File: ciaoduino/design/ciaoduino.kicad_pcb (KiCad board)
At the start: 2 copper layers, 8 parts, among them P1 ICSP, SW1 SW_PUSH, SW2 SW_PUSH, X1 CRYSTAL_SMD

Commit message: Make more realistic board.
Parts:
- added P2: CONN_01X02, Pin_Headers:Pin_Header_Angled_1x02, F.Cu at (142.2, 64.8)
- added P3: USB_OTG, Connect:USB_Mini-B, F.Cu at (130.8, 72.4)
- added P4: CONN_01X06, Pin_Headers:Pin_Header_Straight_1x06, F.Cu at (154.9, 95.2)
- added R3: R, Resistors_SMD:R_0603, F.Cu at (139.7, 73.7)
- added R4: R, Resistors_SMD:R_0603, F.Cu at (139.7, 71.1)
- added U2: ATmega32U4-AU, Housings_QFP:TQFP-44_10x10mm_Pitch0.8mm, F.Cu at (151.1, 74.9)
- C1, C2: footprint Capacitors_SMD:C_0603_HandSoldering -> Capacitors_SMD:C_0603
- R1, R2: footprint Resistors_SMD:R_0603_HandSoldering -> Resistors_SMD:R_0603
- moved R2 52.9 mm to (165.1, 67.3)
- moved SW1 39.8 mm to (170.2, 81.3)
- moved R1 31.2 mm to (165.1, 87.6)
- moved C1 25.7 mm to (156.2, 90.2), turned to 270 degrees
- moved SW2 24.0 mm to (170.2, 72.4)
- moved C2 21.8 mm to (146.1, 90.2), turned to 270 degrees
- moved X1 15.1 mm to (151.1, 90.2), turned to 180 degrees
- moved P1 6.48 mm to (171.4, 87.6)
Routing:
- net VCC: track 0.00 -> 78.9 mm, vias 0 -> 2
- net Net-(R1-Pad2): track 0.00 -> 21.2 mm, vias 0 -> 2
- net Net-(R2-Pad2): track 0.00 -> 20.5 mm
- net usart_cts: track 0.00 -> 19.0 mm
- net usart_tx: track 0.00 -> 18.0 mm
- net usart_rx: track 0.00 -> 17.3 mm
- net Net-(C1-Pad1): track 0.00 -> 12.2 mm
- net Net-(C2-Pad1): track 0.00 -> 11.9 mm
- added copper zone on F.Cu, net GND
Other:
- board outline added: 58.4 x 36.8 mm

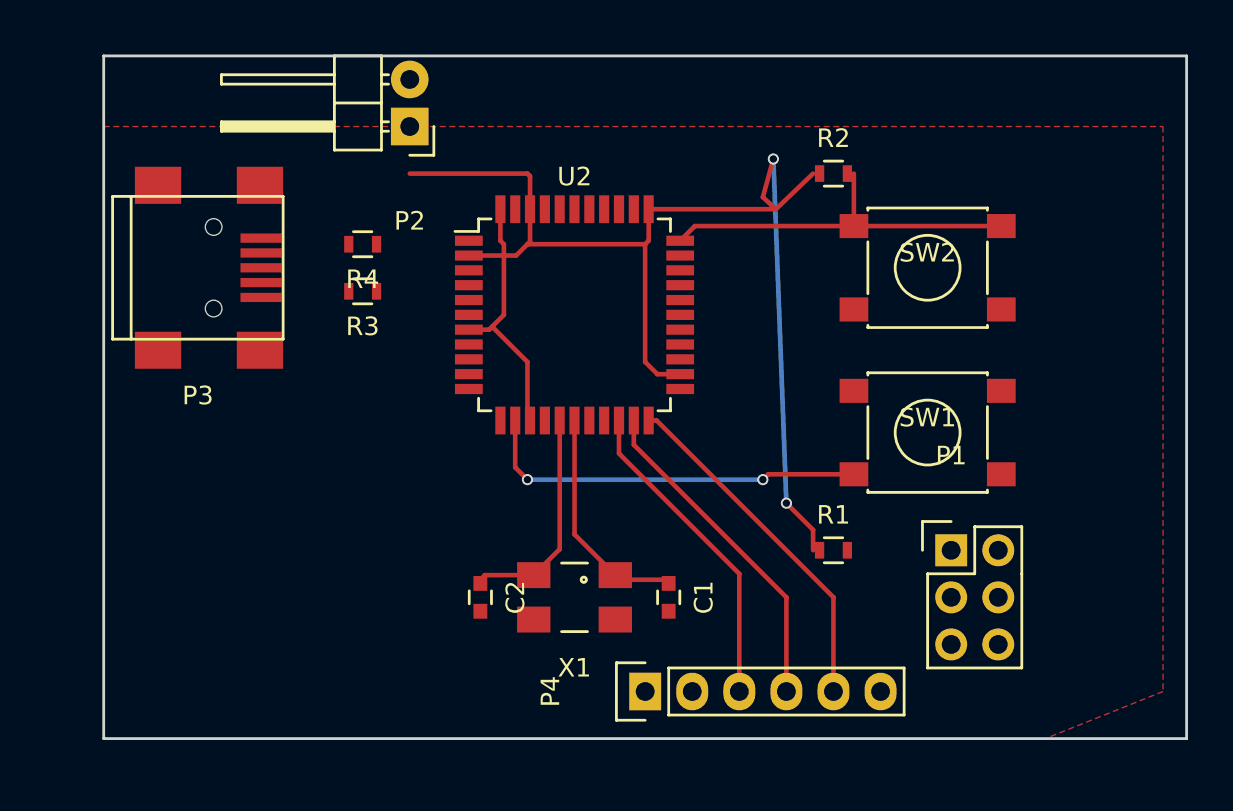
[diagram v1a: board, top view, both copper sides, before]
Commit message: Add protocol connectors.
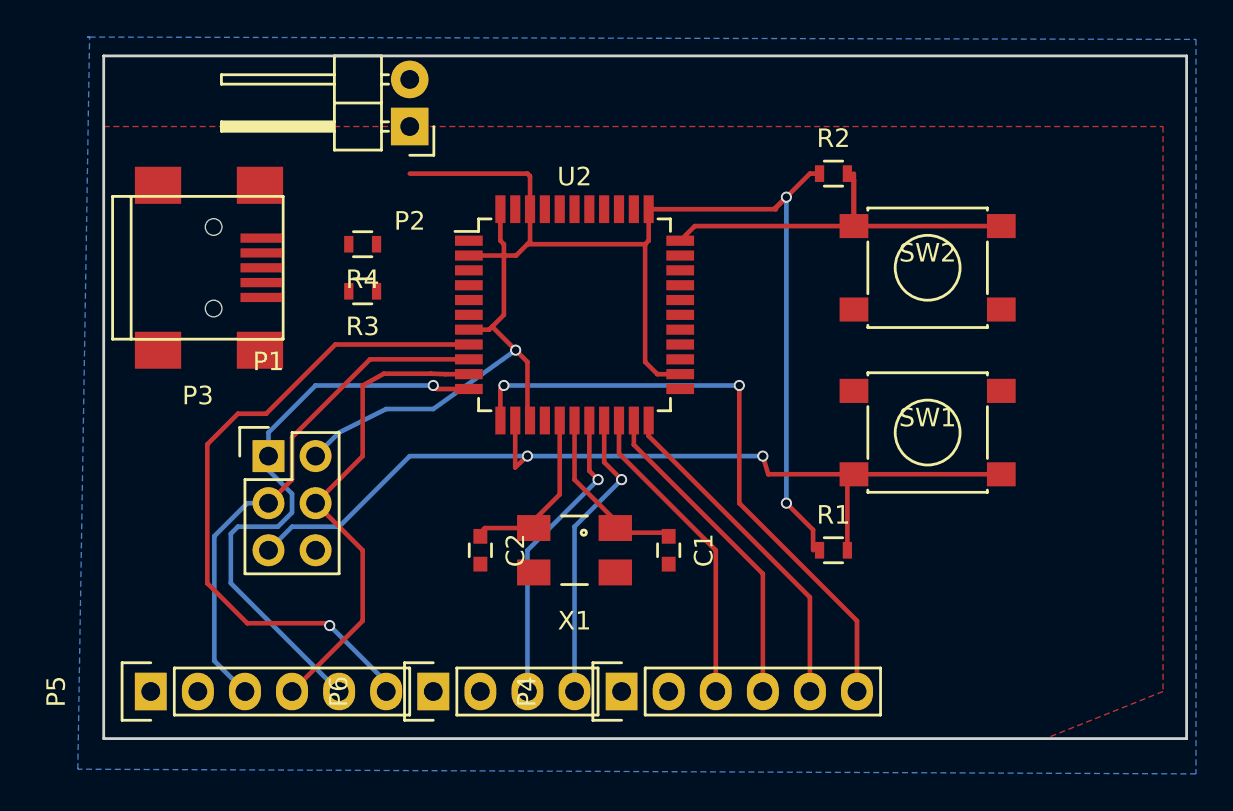
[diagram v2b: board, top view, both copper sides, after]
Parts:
- added P5: CONN_01X06, Pin_Headers:Pin_Header_Straight_1x06, F.Cu at (128.3, 95.2)
- added P6: CONN_01X04, Pin_Headers:Pin_Header_Straight_1x04, F.Cu at (143.5, 95.2)
- moved P1 37.2 mm to (134.6, 82.5)
- moved C1 2.54 mm to (156.2, 87.6)
- moved C2 2.54 mm to (146.1, 87.6)
- moved X1 2.54 mm to (151.1, 87.6)
- moved P4 1.27 mm to (153.7, 95.2)
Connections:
- P1 pad 2: Net-(P1-Pad2) -> VCC
- P1 pad 3: Net-(P1-Pad3) -> SCLK
- P1 pad 4: Net-(P1-Pad4) -> MOSI
- P1 pad 5: Net-(P1-Pad5) -> RESET
- P1 pad 6: Net-(P1-Pad6) -> GND
- P3 pad 5: Net-(P3-Pad5) -> GND
- R1 pad 2: Net-(R1-Pad2) -> RESET
- SW1 pad 2: Net-(R1-Pad2) -> RESET
- U2 pad 10: Net-(U2-Pad10) -> MOSI
- U2 pad 11: Net-(U2-Pad11) -> MISO
- U2 pad 13: Net-(R1-Pad2) -> RESET
- U2 pad 18: Net-(U2-Pad18) -> SCL
- U2 pad 19: Net-(U2-Pad19) -> SDA
- U2 pad 8: Net-(U2-Pad8) -> SS
- U2 pad 9: Net-(U2-Pad9) -> SCLK
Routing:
- net RESET: track 0.00 -> 50.0 mm, vias 0 -> 2
- net SS: track 0.00 -> 36.2 mm, vias 0 -> 1
- net usart_rts: track 0.00 -> 33.8 mm, vias 0 -> 2
- net MISO: track 0.00 -> 31.5 mm, vias 0 -> 1
- net SCLK: track 0.00 -> 28.1 mm
- net MOSI: track 0.00 -> 26.1 mm
- net Net-(R1-Pad2): track 21.2 -> 0.00 mm, vias 2 -> 0
- net SCL: track 0.00 -> 16.4 mm, vias 0 -> 1
- net SDA: track 0.00 -> 16.1 mm, vias 0 -> 1
- net VCC: track 78.9 -> 87.7 mm, vias 2 -> 3
- net Net-(R2-Pad2): track 20.5 -> 23.5 mm
- net Net-(C1-Pad1): track 12.2 -> 9.70 mm
- net Net-(C2-Pad1): track 11.9 -> 9.36 mm
- net usart_cts: track 19.0 -> 18.2 mm
- net usart_tx: track 18.0 -> 17.5 mm
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- added copper zone on B.Cu, net GND
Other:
- net class Default: trace_width 0.25 -> 0.1524
- rule pad_to_mask_clearance: 0.2 -> 0.1
- rule trace_min: 0.2 -> 0.1524

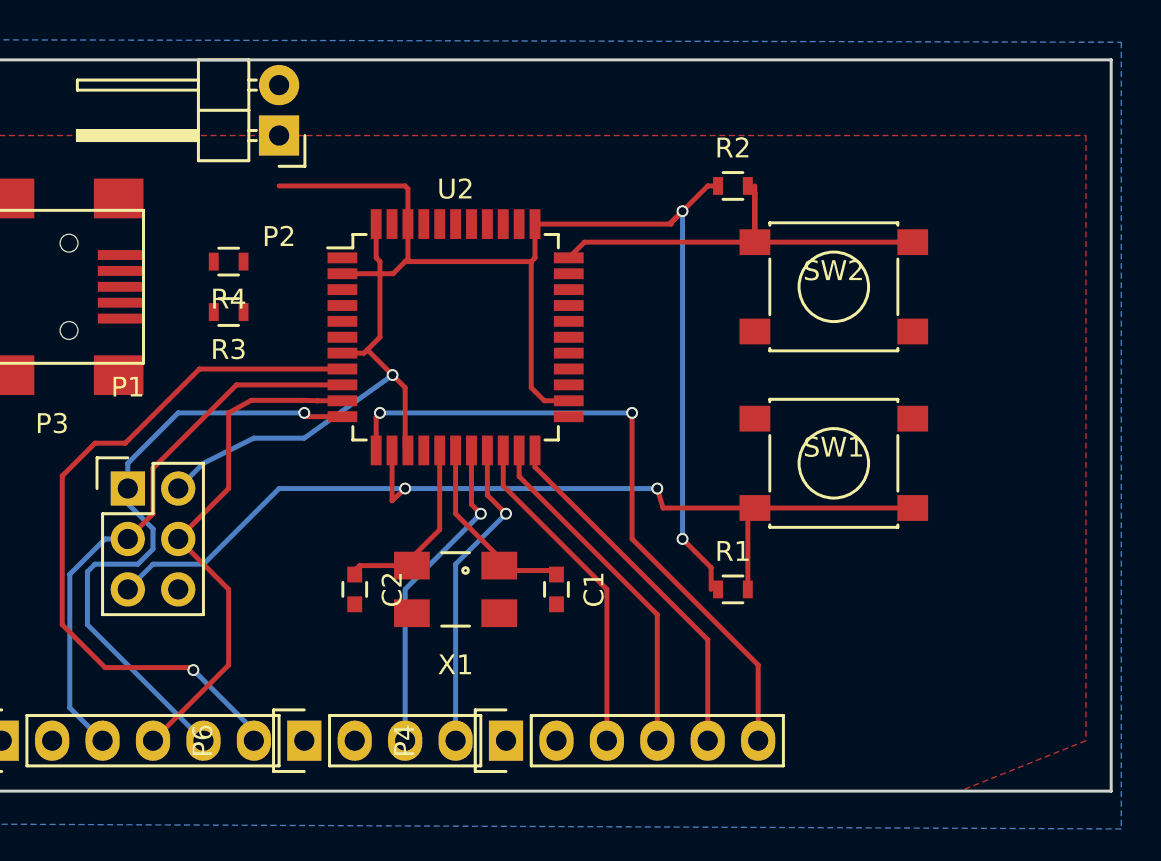
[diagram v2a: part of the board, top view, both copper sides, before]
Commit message: Route ADC related IO pins.
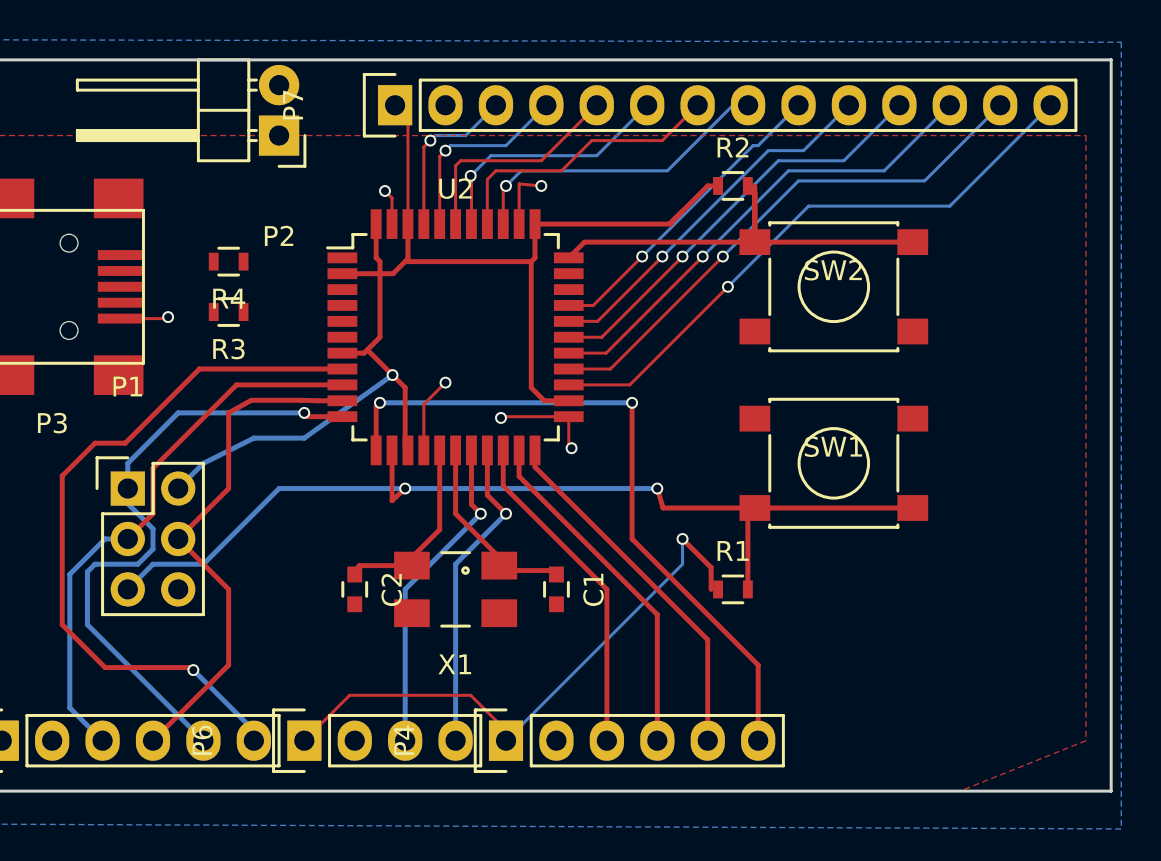
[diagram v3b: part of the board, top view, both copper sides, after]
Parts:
- added P7: CONN_01X14, Pin_Headers:Pin_Header_Straight_1x14, F.Cu at (148.1, 63.2)
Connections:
- U2 pad 25: Net-(U2-Pad25) -> ADC8
- U2 pad 26: Net-(U2-Pad26) -> ADC9
- U2 pad 27: Net-(U2-Pad27) -> ADC10
- U2 pad 28: Net-(U2-Pad28) -> ADC11
- U2 pad 29: Net-(U2-Pad29) -> ADC12
- U2 pad 30: Net-(U2-Pad30) -> ADC13
- U2 pad 36: Net-(U2-Pad36) -> ADC7
- U2 pad 37: Net-(U2-Pad37) -> ADC6
- U2 pad 38: Net-(U2-Pad38) -> ADC5
- U2 pad 39: Net-(U2-Pad39) -> ADC4
- U2 pad 40: Net-(U2-Pad40) -> ADC1
- U2 pad 41: Net-(U2-Pad41) -> ADC0
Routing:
- net ADC8: track 0.00 -> 30.1 mm, vias 0 -> 1
- net ADC9: track 0.00 -> 27.2 mm, vias 0 -> 1
- net ADC10: track 0.00 -> 24.4 mm, vias 0 -> 1
- net ADC11: track 0.00 -> 21.5 mm, vias 0 -> 1
- net ADC12: track 0.00 -> 18.6 mm, vias 0 -> 1
- net GND: track 0.00 -> 16.3 mm, vias 0 -> 6
- net ADC7: track 0.00 -> 15.9 mm, vias 0 -> 1
- net ADC13: track 0.00 -> 15.7 mm, vias 0 -> 1
- net ADC6: track 0.00 -> 14.4 mm
- net ADC5: track 0.00 -> 12.8 mm, vias 0 -> 1
- net ADC4: track 0.00 -> 11.3 mm
- net ADC1: track 0.00 -> 9.85 mm, vias 0 -> 1
- net ADC0: track 0.00 -> 8.38 mm, vias 0 -> 1
- net VCC: track 87.7 -> 95.3 mm, vias 3 -> 2
- net usart_rts: track 33.8 -> 34.8 mm

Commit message: Update ciaoduino design.
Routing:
- net VCC: track 95.3 -> 132.5 mm, vias 2 -> 3
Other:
- board size 58.4 x 36.8 mm -> 58.4 x 37.3 mm
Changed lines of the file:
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@@
   (general
     (links 73)
-    (no_connects 12)
-    (area 122.045 58.137666 184.658001 100.358333)
+    (no_connects 8)
+    (area 125.654999 60.884999 184.225001 97.865001)
     (thickness 1.6)
     (drawings 4)
-    (tracks 234)
+    (tracks 246)
     (zones 0)
     (modules 17)
@@
   (gr_line (start 184.15 97.79) (end 125.73 97.79) (angle 90) (layer Edge.Cuts) (width 0.15))
   (gr_line (start 184.15 60.96) (end 184.15 97.79) (angle 90) (layer Edge.Cuts) (width 0.15))
-  (gr_line (start 125.73 60.96) (end 184.15 60.96) (angle 90) (layer Edge.Cuts) (width 0.15))
+  (gr_line (start 125.73 60.452) (end 184.15 60.452) (angle 90) (layer Edge.Cuts) (width 0.15))
   (segment (start 153.32964 86.43112) (end 153.32964 86.01964) (width 0.25) (layer F.Cu) (net 1))
   (segment (start 153.32964 86.01964) (end 151.13 83.82) (width 0.25) (layer F.Cu) (net 1))
@@
   (via (at 143.51 78.74) (size 0.6) (drill 0.4) (layers F.Cu B.Cu) (net 4))
   (segment (start 143.7 78.93) (end 143.51 78.74) (width 0.25) (layer F.Cu) (net 4))
+  (segment (start 162.56 85.09) (end 162.56 81.534) (width 0.1524) (layer B.Cu) (net 5))
+  (via (at 154.94 77.216) (size 0.6) (drill 0.4) (layers F.Cu B.Cu) (net 5))
+  (segment (start 160.782 77.216) (end 154.94 77.216) (width 0.1524) (layer B.Cu) (net 5))
+  (segment (start 161.29 77.724) (end 160.782 77.216) (width 0.1524) (layer B.Cu) (net 5))
+  (segment (start 161.29 80.264) (end 161.29 77.724) (width 0.1524) (layer B.Cu) (net 5))
+  (segment (start 162.56 81.534) (end 161.29 80.264) (width 0.1524) (layer B.Cu) (net 5))
+  (segment (start 128.27 95.25) (end 129.794 96.774) (width 0.1524) (layer F.Cu) (net 5))
+  (segment (start 141.986 96.774) (end 143.51 95.25) (width 0.1524) (layer F.Cu) (net 5))
+  (segment (start 129.794 96.774) (end 141.986 96.774) (width 0.1524) (layer F.Cu) (net 5))
+  (segment (start 142.24 62.23) (end 147.066 62.23) (width 0.1524) (layer F.Cu) (net 5))
+  (segment (start 147.066 62.23) (end 148.082 63.246) (width 0.1524) (layer F.Cu) (net 5))
   (segment (start 148.73 69.23) (end 148.73 63.894) (width 0.1524) (layer F.Cu) (net 5))
   (segment (start 148.73 63.894) (end 148.082 63.246) (width 0.1524) (layer F.Cu) (net 5))
@@
   (segment (start 162.56 85.09) (end 164 86.53) (width 0.25) (layer F.Cu) (net 5))
   (segment (start 164 86.53) (end 164 87.63) (width 0.25) (layer F.Cu) (net 5))
-  (segment (start 154.94 71.12) (end 154.94 77.47) (width 0.25) (layer F.Cu) (net 5))
+  (segment (start 154.94 71.12) (end 154.94 77.216) (width 0.25) (layer F.Cu) (net 5))
+  (segment (start 154.94 77.216) (end 154.94 77.47) (width 0.25) (layer F.Cu) (net 5))
+  (segment (start 154.94 77.47) (end 155.6 78.13) (width 0.25) (layer F.Cu) (net 5))
   (segment (start 155.6 78.13) (end 156.83 78.13) (width 0.25) (layer F.Cu) (net 5))
-  (segment (start 154.94 77.47) (end 155.6 78.13) (width 0.25) (layer F.Cu) (net 5))
   (segment (start 155.13 69.23) (end 155.13 70.93) (width 0.25) (layer F.Cu) (net 5))
   (segment (start 154.94 71.12) (end 148.59 71.12) (width 0.25) (layer F.Cu) (net 5))
@@
   (via (at 153.67 67.31) (size 0.6) (drill 0.4) (layers F.Cu B.Cu) (net 35))
   (segment (start 165.1 63.246) (end 165.862 63.246) (width 0.1524) (layer B.Cu) (net 35))
-  (segment (start 156.83 77.33) (end 159.906 77.33) (width 0.1524) (layer F.Cu) (net 36) (status 400000))
-  (segment (start 176.022 68.326) (end 181.102 63.246) (width 0.1524) (layer B.Cu) (net 36) (status 800000))
+  (segment (start 156.83 77.33) (end 159.906 77.33) (width 0.1524) (layer F.Cu) (net 36))
+  (segment (start 176.022 68.326) (end 181.102 63.246) (width 0.1524) (layer B.Cu) (net 36))
   (segment (start 168.91 68.326) (end 176.022 68.326) (width 0.1524) (layer B.Cu) (net 36))
   (segment (start 164.846 72.39) (end 168.91 68.326) (width 0.1524) (layer B.Cu) (net 36))
   (via (at 164.846 72.39) (size 0.6) (drill 0.4) (layers F.Cu B.Cu) (net 36))
   (segment (start 159.906 77.33) (end 164.846 72.39) (width 0.1524) (layer F.Cu) (net 36))
-  (segment (start 156.83 76.53) (end 158.928 76.53) (width 0.1524) (layer F.Cu) (net 37) (status 400000))
-  (segment (start 174.752 67.056) (end 178.562 63.246) (width 0.1524) (layer B.Cu) (net 37) (status 800000))
+  (segment (start 156.83 76.53) (end 158.928 76.53) (width 0.1524) (layer F.Cu) (net 37))
+  (segment (start 174.752 67.056) (end 178.562 63.246) (width 0.1524) (layer B.Cu) (net 37))
   (segment (start 168.402 67.056) (end 174.752 67.056) (width 0.1524) (layer B.Cu) (net 37))
   (segment (start 164.592 70.866) (end 168.402 67.056) (width 0.1524) (layer B.Cu) (net 37))
   (via (at 164.592 70.866) (size 0.6) (drill 0.4) (layers F.Cu B.Cu) (net 37))
   (segment (start 158.928 76.53) (end 164.592 70.866) (width 0.1524) (layer F.Cu) (net 37))
-  (segment (start 156.83 75.73) (end 158.712 75.73) (width 0.1524) (layer F.Cu) (net 38) (status 400000))
-  (segment (start 172.72 66.548) (end 176.022 63.246) (width 0.1524) (layer B.Cu) (net 38) (status 800000))
+  (segment (start 156.83 75.73) (end 158.712 75.73) (width 0.1524) (layer F.Cu) (net 38))
+  (segment (start 172.72 66.548) (end 176.022 63.246) (width 0.1524) (layer B.Cu) (net 38))
   (segment (start 167.894 66.548) (end 172.72 66.548) (width 0.1524) (layer B.Cu) (net 38))
   (segment (start 163.576 70.866) (end 167.894 66.548) (width 0.1524) (layer B.Cu) (net 38))
   (via (at 163.576 70.866) (size 0.6) (drill 0.4) (layers F.Cu B.Cu) (net 38))
   (segment (start 158.712 75.73) (end 163.576 70.866) (width 0.1524) (layer F.Cu) (net 38))
-  (segment (start 156.83 74.93) (end 158.496 74.93) (width 0.1524) (layer F.Cu) (net 39) (status 400000))
-  (segment (start 170.688 66.04) (end 173.482 63.246) (width 0.1524) (layer B.Cu) (net 39) (status 800000))
+  (segment (start 156.83 74.93) (end 158.496 74.93) (width 0.1524) (layer F.Cu) (net 39))
+  (segment (start 170.688 66.04) (end 173.482 63.246) (width 0.1524) (layer B.Cu) (net 39))
   (segment (start 167.386 66.04) (end 170.688 66.04) (width 0.1524) (layer B.Cu) (net 39))
   (segment (start 162.56 70.866) (end 167.386 66.04) (width 0.1524) (layer B.Cu) (net 39))
   (via (at 162.56 70.866) (size 0.6) (drill 0.4) (layers F.Cu B.Cu) (net 39))
   (segment (start 158.496 74.93) (end 162.56 70.866) (width 0.1524) (layer F.Cu) (net 39))
-  (segment (start 156.83 74.13) (end 158.28 74.13) (width 0.1524) (layer F.Cu) (net 40) (status 400000))
-  (segment (start 168.656 65.532) (end 170.942 63.246) (width 0.1524) (layer B.Cu) (net 40) (status 800000))
+  (segment (start 156.83 74.13) (end 158.28 74.13) (width 0.1524) (layer F.Cu) (net 40))
+  (segment (start 168.656 65.532) (end 170.942 63.246) (width 0.1524) (layer B.Cu) (net 40))
   (segment (start 166.878 65.532) (end 168.656 65.532) (width 0.1524) (layer B.Cu) (net 40))
   (segment (start 161.544 70.866) (end 166.878 65.532) (width 0.1524) (layer B.Cu) (net 40))
   (via (at 161.544 70.866) (size 0.6) (drill 0.4) (layers F.Cu B.Cu) (net 40))
   (segment (start 158.28 74.13) (end 161.544 70.866) (width 0.1524) (layer F.Cu) (net 40))
-  (segment (start 156.83 73.33) (end 158.064 73.33) (width 0.1524) (layer F.Cu) (net 41) (status 400000))
-  (segment (start 166.37 65.278) (end 168.402 63.246) (width 0.1524) (layer B.Cu) (net 41) (status 800000))
+  (segment (start 156.83 73.33) (end 158.064 73.33) (width 0.1524) (layer F.Cu) (net 41))
+  (segment (start 166.37 65.278) (end 168.402 63.246) (width 0.1524) (layer B.Cu) (net 41))
   (segment (start 166.116 65.278) (end 166.37 65.278) (width 0.1524) (layer B.Cu) (net 41))
   (segment (start 160.528 70.866) (end 166.116 65.278) (width 0.1524) (layer B.Cu) (net 41))

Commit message: Rework layout.
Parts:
- C1, C2: footprint Capacitors_SMD:C_0603 -> Capacitors_SMD:C_0603_HandSoldering
- P4: footprint Pin_Headers:Pin_Header_Straight_1x06 -> Pin_Headers:Pin_Header_Angled_1x06
- R2: footprint Resistors_SMD:R_0603 -> Resistors_SMD:R_0603_HandSoldering
- SW1: footprint Buttons_Switches_SMD:SW_SPST_PTS645 -> Buttons_Switches_SMD:SW_SPST_KMR2
- SW2: footprint Buttons_Switches_SMD:SW_SPST_PTS645 -> Buttons_Switches_SMD:SW_SPST_EVQP0
- X1: footprint Crystals:Crystal_SMD_0603_4Pads -> Crystals:crystal_FA238-TSX3225
- moved P4 12.7 mm to (165.4, 100.3), turned to 120 degrees
- moved P5 12.5 mm to (139.7, 100.3), turned to 240 degrees
- moved P7 9.94 mm to (138.2, 62.5)
- moved P2 8.89 mm to (133.3, 65.0)
- moved P6 7.91 mm to (148.8, 101.1)
- moved P1 5.36 mm to (134.1, 87.9), turned to 90 degrees
- moved R2 4.37 mm to (161.5, 69.8)
- moved P3 2.54 mm to (130.8, 74.9)
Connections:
- P3 pad 1: Net-(P3-Pad1) -> (no net)
- P3 pad 4: Net-(P3-Pad4) -> (no net)
- U2 pad 1: Net-(U2-Pad1) -> (no net)
- U2 pad 31: Net-(U2-Pad31) -> (no net)
- U2 pad 32: Net-(U2-Pad32) -> (no net)
- U2 pad 5: Net-(U2-Pad5) -> (no net)
- U2 pad 6: Net-(U2-Pad6) -> (no net)
- X1 pad 3: Net-(X1-Pad3) -> GND
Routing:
- net Net-(P3-Pad6): track 0.00 -> 19.9 mm
- net VCC: track 132.5 -> 146.0 mm, vias 3 -> 8
- net usart_cts: track 18.2 -> 27.7 mm, vias 0 -> 2
- net usart_rx: track 16.8 -> 25.4 mm
- net usart_tx: track 17.5 -> 25.7 mm
- net ADC7: track 15.9 -> 7.90 mm, vias 1 -> 0
- net ADC6: track 14.4 -> 7.03 mm
- net SS: track 36.2 -> 29.3 mm, vias 1 -> 0
- net ADC9: track 27.2 -> 20.9 mm
- net Net-(P3-Pad2): track 0.00 -> 6.08 mm
- net Net-(R2-Pad2): track 23.5 -> 17.4 mm
- net SDA: track 16.1 -> 22.0 mm, vias 1 -> 0
- net ADC10: track 24.4 -> 18.7 mm
- net ADC5: track 12.8 -> 7.18 mm, vias 1 -> 0
- net Net-(R4-Pad1): track 0.00 -> 5.56 mm
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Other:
- board size 58.4 x 37.3 mm -> 76.4 x 76.4 mm
- board text added: "UART"
